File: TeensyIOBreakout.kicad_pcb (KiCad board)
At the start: 2 copper layers, 41 x 32.5 mm, 9 parts, among them J1 Conn_01x14_Male, J2 Conn_01x14_Male, J3 Conn_01x14_Male, J4 Conn_01x14_Male, J5 Conn_01x03_Male, J6 Conn_01x05_Male, J7 Conn_01x02_Male, U1 Teensy3.2

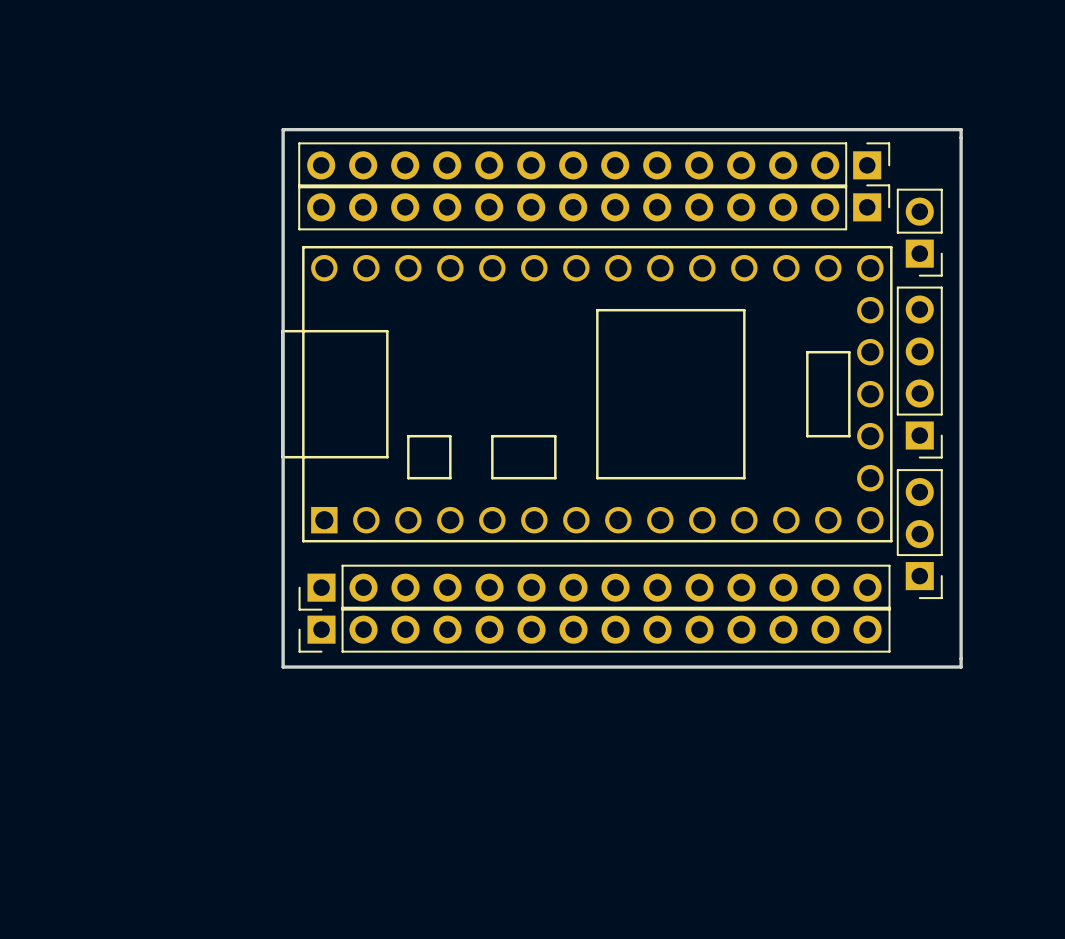
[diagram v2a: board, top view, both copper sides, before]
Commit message: Made board bigger, added moutning holes, front labels
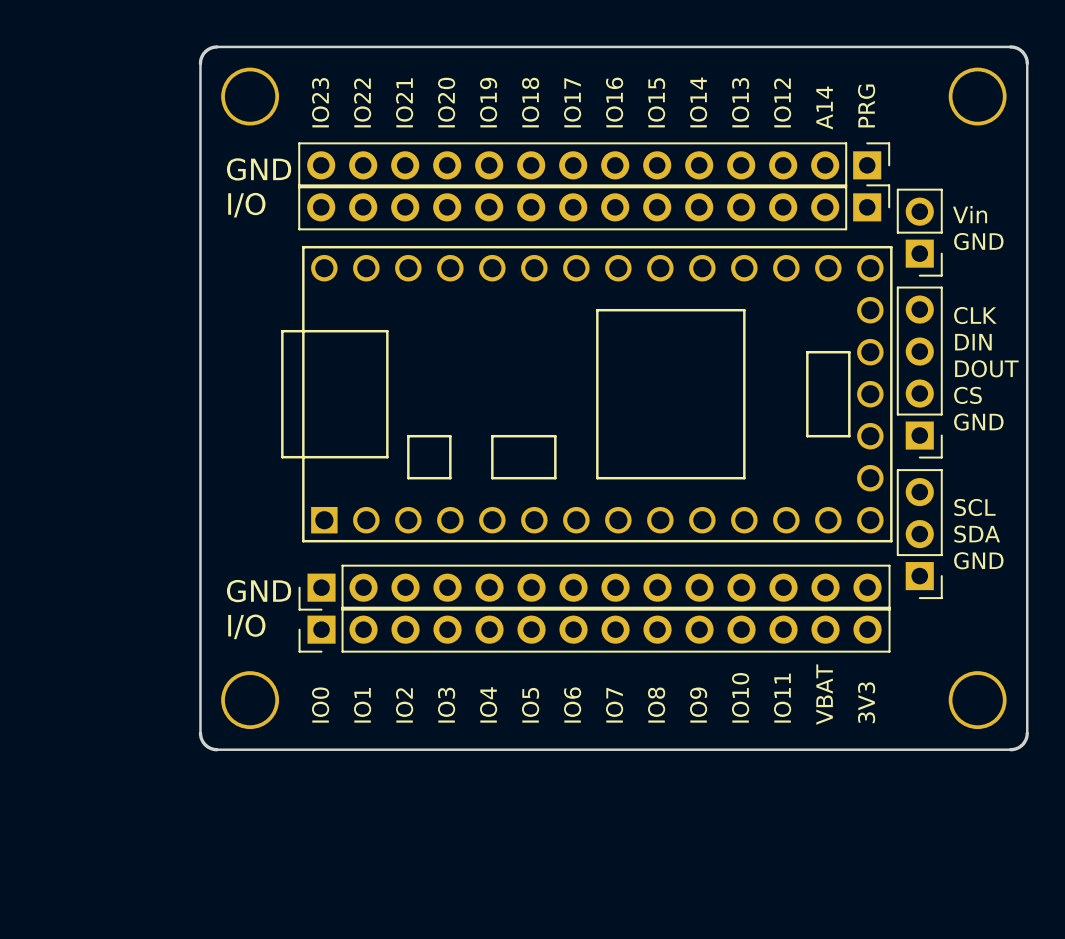
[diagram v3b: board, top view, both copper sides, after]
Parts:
- added REF**: mount, mount:mount, F.Cu at (153.0, 57.0)
- added REF**: mount, mount:mount, F.Cu at (153.0, 20.5)
- added REF**: mount, mount:mount, F.Cu at (109.0, 20.5)
- added REF**: mount, mount:mount, F.Cu at (109.0, 57.0)
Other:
- board size 41 x 32.5 mm -> 50 x 42.5 mm
- board text added: "3V3"
- board text added: "A14"
- board text added: "CLK DIN DOUT CS GND"
- board text added: "GND I/O"
- board text added: "IO0"
- board text added: "IO1"
- board text added: "IO10"
- board text added: "IO11"
- board text added: "IO12"
- board text added: "IO13"
- board text added: "IO14"
- board text added: "IO15"
- board text added: "IO16"
- board text added: "IO17"
- board text added: "IO18"
- board text added: "IO19"
- board text added: "IO2"
- board text added: "IO20"
- board text added: "IO21"
- board text added: "IO22"
- board text added: "IO23"
- board text added: "IO3"
- board text added: "IO4"
- board text added: "IO5"
- board text added: "IO6"
- board text added: "IO7"
- board text added: "IO8"
- board text added: "IO9"
- board text added: "PRG"
- board text added: "SCL SDA GND"
- board text added: "VBAT"
- board text added: "Vin GND"
- board text removed: "Cl.Da.G"
- board text removed: "Cl.Di.Do.Cs.G"
- board text removed: "IO0 \/ IO11 VBAT 3V3"
- board text removed: "IO23 \/ IO12 A14 PROG"
- board text removed: "Vin.G"
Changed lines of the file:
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@@
   (general
     (thickness 1.6)
-    (drawings 13)
+    (drawings 41)
     (tracks 0)
     (zones 0)
-    (modules 9)
+    (modules 13)
     (nets 34)
   )
@@
     (mod_text_size 1 1)
     (mod_text_width 0.15)
-    (pad_size 1.524 1.524)
-    (pad_drill 0.762)
+    (pad_size 3.5 3.5)
+    (pad_drill 3.048)
     (pad_to_mask_clearance 0.2)
     (aux_axis_origin 0 0)
@@
     (add_net VBAT)
     (add_net Vin)
+  )
+  (module mount:mount (layer F.Cu)
+    (at 153 57)
+    (descr "3mm mount hole for 5.25mm standoff")
+    (tags DEV)
+    (fp_text reference REF** (at 0 -3.048) (layer F.SilkS) hide
+      (effects (font (size 1 1) (thickness 0.15)))
+    )
+    (fp_text value mount (at 0 3) (layer F.Fab) hide
+      (effects (font (size 1 1) (thickness 0.15)))
+    )
+    (fp_circle (center 0 0) (end 2.6 0) (layer F.CrtYd) (width 0.05))
+    (pad "" thru_hole circle (at 0 0) (size 3.5 3.5) (drill 3.048) (layers *.Cu *.Mask))
+  )
+  (module mount:mount (layer F.Cu)
+    (at 153 20.5)
+    (descr "3mm mount hole for 5.25mm standoff")
+    (tags DEV)
+    (fp_text reference REF** (at 0 -3.048) (layer F.SilkS) hide
+      (effects (font (size 1 1) (thickness 0.15)))
+    )
+    (fp_text value mount (at 0 3) (layer F.Fab) hide
+      (effects (font (size 1 1) (thickness 0.15)))
+    )
+    (fp_circle (center 0 0) (end 2.6 0) (layer F.CrtYd) (width 0.05))
+    (pad "" thru_hole circle (at 0 0) (size 3.5 3.5) (drill 3.048) (layers *.Cu *.Mask))
+  )
+  (module mount:mount (layer F.Cu)
+    (at 109 20.5)
+    (descr "3mm mount hole for 5.25mm standoff")
+    (tags DEV)
+    (fp_text reference REF** (at 0 -3.048) (layer F.SilkS) hide
+      (effects (font (size 1 1) (thickness 0.15)))
+    )
+    (fp_text value mount (at 0 3) (layer F.Fab) hide
+      (effects (font (size 1 1) (thickness 0.15)))
+    )
+    (fp_circle (center 0 0) (end 2.6 0) (layer F.CrtYd) (width 0.05))
+    (pad "" thru_hole circle (at 0 0) (size 3.5 3.5) (drill 3.048) (layers *.Cu *.Mask))
   )
   (module Pin_Headers:Pin_Header_Straight_1x14_Pitch2.54mm (layer F.Cu)
@@
       (xy 0.280132 4.064859)) (layer B.SilkS) (width 0.01))
   )
-  (gr_text Vin.G (at 144 35 90) (layer B.SilkS)
-    (effects (font (size 1.1 1) (thickness 0.2)) (justify mirror))
-  )
-  (gr_text Cl.Di.Do.Cs.G (at 142 38.5 90) (layer B.SilkS)
-    (effects (font (size 1.1 1) (thickness 0.2)) (justify mirror))
-  )
-  (gr_text Cl.Da.G (at 144 42 90) (layer B.SilkS)
-    (effects (font (size 1.1 1) (thickness 0.2)) (justify mirror))
-  )
-  (gr_text "IO0\n\\/\nIO11\nVBAT\n3V3" (at 130 42.5 90) (layer B.SilkS)
-    (effects (font (size 1.1 1.1) (thickness 0.2)) (justify mirror))
-  )
-  (gr_text "IO23\n\\/\nIO12\nA14\nPROG" (at 130 34.5 90) (layer B.SilkS)
-    (effects (font (size 1.1 1.1) (thickness 0.2)) (justify mirror))
-  )
-  (dimension 41 (width 0.3) (layer Dwgs.User)
-    (gr_text "41.000 mm" (at 131.5 18.9) (layer Dwgs.User)
-      (effects (font (size 1.5 1.5) (thickness 0.3)))
-    )
-    (feature1 (pts (xy 152 22.5) (xy 152 20.413579)))
-    (feature2 (pts (xy 111 22.5) (xy 111 20.413579)))
-    (crossbar (pts (xy 111 21) (xy 152 21)))
-    (arrow1a (pts (xy 152 21) (xy 150.873496 21.586421)))
-    (arrow1b (pts (xy 152 21) (xy 150.873496 20.413579)))
-    (arrow2a (pts (xy 111 21) (xy 112.126504 21.586421)))
-    (arrow2b (pts (xy 111 21) (xy 112.126504 20.413579)))
-  )
-  (dimension 32.5 (width 0.3) (layer Dwgs.User)
-    (gr_text "32.500 mm" (at 156.1 38.75 270) (layer Dwgs.User)
-      (effects (font (size 1.5 1.5) (thickness 0.3)))
-    )
-    (feature1 (pts (xy 152 55) (xy 154.586421 55)))
-    (feature2 (pts (xy 152 22.5) (xy 154.586421 22.5)))
-    (crossbar (pts (xy 154 22.5) (xy 154 55)))
-    (arrow1a (pts (xy 154 55) (xy 153.413579 53.873496)))
-    (arrow1b (pts (xy 154 55) (xy 154.586421 53.873496)))
-    (arrow2a (pts (xy 154 22.5) (xy 153.413579 23.626504)))
-    (arrow2b (pts (xy 154 22.5) (xy 154.586421 23.626504)))
-  )
-  (gr_line (start 152 22.5) (end 152 23) (layer Edge.Cuts) (width 0.2))
-  (gr_line (start 111 22.5) (end 152 22.5) (layer Edge.Cuts) (width 0.2))
-  (gr_line (start 111 55) (end 111 22.5) (layer Edge.Cuts) (width 0.2))
-  (gr_line (start 152 55) (end 111 55) (layer Edge.Cuts) (width 0.2))
-  (gr_line (start 152 54.5) (end 152 55) (layer Edge.Cuts) (width 0.2))
-  (gr_line (start 152 23) (end 152 54.5) (layer Edge.Cuts) (width 0.2))
+  (module mount:mount (layer F.Cu)
+    (at 109 57)
+    (descr "3mm mount hole for 5.25mm standoff")
+    (tags DEV)
+    (fp_text reference REF** (at 0 -3.048) (layer F.SilkS) hide
+      (effects (font (size 1 1) (thickness 0.15)))
+    )
+    (fp_text value mount (at 0 3) (layer F.Fab) hide
+      (effects (font (size 1 1) (thickness 0.15)))
+    )
+    (fp_circle (center 0 0) (end 2.6 0) (layer F.CrtYd) (width 0.05))
+    (pad "" thru_hole circle (at 0 0) (size 3.5 3.5) (drill 3.048) (layers *.Cu *.Mask))
+  )
+  (gr_text "IO8\n" (at 133.62 58.5 90) (layer F.SilkS)
+    (effects (font (size 1 1) (thickness 0.175)) (justify left))
+  )
+  (gr_text "IO9\n" (at 136.16 58.5 90) (layer F.SilkS)
+    (effects (font (size 1 1) (thickness 0.175)) (justify left))
+  )
+  (gr_text "IO11\n" (at 141.24 58.5 90) (layer F.SilkS)
+    (effects (font (size 1 1) (thickness 0.175)) (justify left))
+  )
+  (gr_text 3V3 (at 146.32 58.5 90) (layer F.SilkS)
+    (effects (font (size 1 1) (thickness 0.175)) (justify left))
+  )
+  (gr_text IO7 (at 131.08 58.5 90) (layer F.SilkS)
+    (effects (font (size 1 1) (thickness 0.175)) (justify left))
+  )
+  (gr_text "IO10\n" (at 138.7 58.5 90) (layer F.SilkS)
+    (effects (font (size 1 1) (thickness 0.175)) (justify left))
+  )
+  (gr_text "IO4\n" (at 123.46 58.5 90) (layer F.SilkS)
+    (effects (font (size 1 1) (thickness 0.175)) (justify left))
+  )
+  (gr_text VBAT (at 143.78 58.5 90) (layer F.SilkS)
+    (effects (font (size 1 1) (thickness 0.175)) (justify left))
+  )
+  (gr_text IO6 (at 128.54 58.5 90) (layer F.SilkS)
+    (effects (font (size 1 1) (thickness 0.175)) (justify left))
+  )
+  (gr_text IO5 (at 126 58.5 90) (layer F.SilkS)
+    (effects (font (size 1 1) (thickness 0.175)) (justify left))
+  )
+  (gr_text IO2 (at 118.38 58.5 90) (layer F.SilkS)
+    (effects (font (size 1 1) (thickness 0.175)) (justify left))
+  )
+  (gr_text "IO3\n" (at 120.92 58.5 90) (layer F.SilkS)
+    (effects (font (size 1 1) (thickness 0.175)) (justify left))
+  )
+  (gr_text "IO1\n" (at 115.84 58.5 90) (layer F.SilkS)
+    (effects (font (size 1 1) (thickness 0.175)) (justify left))
+  )
+  (gr_text "IO0\n" (at 113.3 58.5 90) (layer F.SilkS)
+    (effects (font (size 1 1) (thickness 0.175)) (justify left))
+  )
+  (gr_text PRG (at 146.32 22.5 90) (layer F.SilkS)
+    (effects (font (size 1 1) (thickness 0.175)) (justify left))
+  )
+  (gr_text A14 (at 143.78 22.5 90) (layer F.SilkS)
+    (effects (font (size 1 1) (thickness 0.175)) (justify left))
+  )
+  (gr_text "IO12\n" (at 141.24 22.5 90) (layer F.SilkS)
+    (effects (font (size 1 1) (thickness 0.175)) (justify left))
+  )
+  (gr_text "IO13\n" (at 138.7 22.5 90) (layer F.SilkS)
+    (effects (font (size 1 1) (thickness 0.175)) (justify left))
+  )
+  (gr_text "IO14\n" (at 136.16 22.5 90) (layer F.SilkS)
+    (effects (font (size 1 1) (thickness 0.175)) (justify left))
+  )
+  (gr_text "IO15\n" (at 133.62 22.5 90) (layer F.SilkS)
+    (effects (font (size 1 1) (thickness 0.175)) (justify left))
+  )
+  (gr_text "IO16\n" (at 131.08 22.5 90) (layer F.SilkS)
+    (effects (font (size 1 1) (thickness 0.175)) (justify left))
+  )
+  (gr_text IO17 (at 128.54 22.5 90) (layer F.SilkS)
+    (effects (font (size 1 1) (thickness 0.175)) (justify left))
+  )
+  (gr_text "IO18\n" (at 126 22.5 90) (layer F.SilkS)
+    (effects (font (size 1 1) (thickness 0.175)) (justify left))
+  )
+  (gr_text "IO19\n" (at 123.46 22.5 90) (layer F.SilkS)
+    (effects (font (size 1 1) (thickness 0.175)) (justify left))
+  )
+  (gr_text "IO20\n" (at 120.92 22.5 90) (layer F.SilkS)
+    (effects (font (size 1 1) (thickness 0.175)) (justify left))
+  )
+  (gr_text "IO21\n" (at 118.38 22.5 90) (layer F.SilkS)
+    (effects (font (size 1 1) (thickness 0.175)) (justify left))
+  )
+  (gr_text "IO22\n" (at 115.84 22.5 90) (layer F.SilkS)
+    (effects (font (size 1 1) (thickness 0.175)) (justify left))
+  )
+  (gr_text "IO23\n" (at 113.3 22.5 90) (layer F.SilkS)
+    (effects (font (size 1 1) (thickness 0.175)) (justify left))
+  )
+  (gr_text "GND\nI/O" (at 107.5 51.5) (layer F.SilkS)
+    (effects (font (size 1.3 1.3) (thickness 0.2)) (justify left))
+  )
+  (gr_text "GND\nI/O" (at 107.5 26) (layer F.SilkS)
+    (effects (font (size 1.3 1.3) (thickness 0.2)) (justify left))
+  )
+  (gr_text "CLK\nDIN\nDOUT\nCS\nGND" (at 151.5 37) (layer F.SilkS)
+    (effects (font (size 1 1) (thickness 0.175)) (justify left))
+  )
+  (gr_text "SCL\nSDA\nGND" (at 151.5 47) (layer F.SilkS)
+    (effects (font (size 1 1) (thickness 0.175)) (justify left))
+  )
+  (gr_line (start 106 18.5) (end 106 59) (layer Edge.Cuts) (width 0.15))
+  (gr_line (start 155 17.5) (end 107 17.5) (layer Edge.Cuts) (width 0.15))
+  (gr_line (start 156 59) (end 156 18.5) (layer Edge.Cuts) (width 0.15))
+  (gr_line (start 107 60) (end 155 60) (layer Edge.Cuts) (width 0.15))
+  (gr_arc (start 107 59) (end 106 59) (angle -90) (layer Edge.Cuts) (width 0.2))
+  (gr_arc (start 107 18.5) (end 107 17.5) (angle -90) (layer Edge.Cuts) (width 0.2))
+  (gr_arc (start 155 18.5) (end 156 18.5) (angle -90) (layer Edge.Cuts) (width 0.2))
+  (gr_arc (start 155 59) (end 155 60) (angle -90) (layer Edge.Cuts) (width 0.2))
+  (gr_text "Vin\nGND" (at 151.5 28.5) (layer F.SilkS)
+    (effects (font (size 1 1) (thickness 0.2)) (justify left))
+  )
 )

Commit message: Added USB cutout, fixed labels.
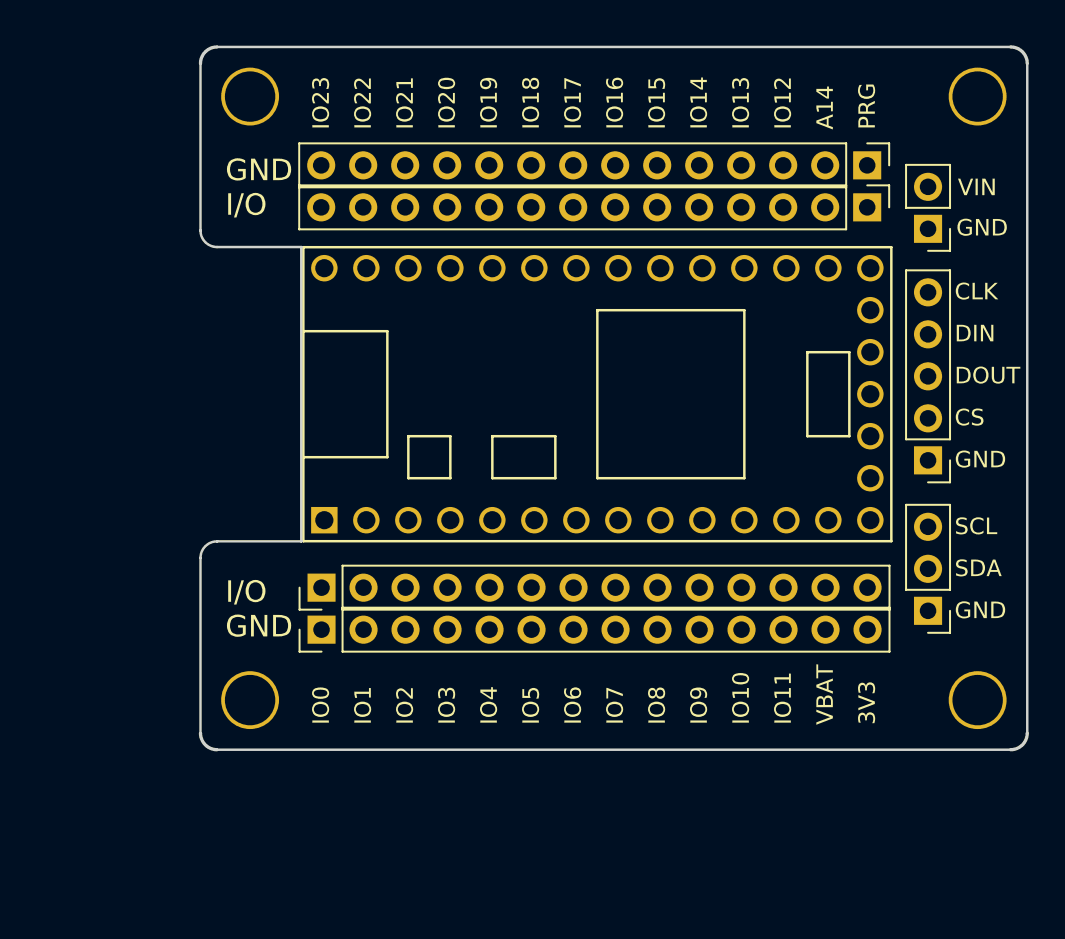
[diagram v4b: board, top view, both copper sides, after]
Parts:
- J6: footprint Pin_Headers:Pin_Header_Straight_1x04_Pitch2.54mm -> Pin_Headers:Pin_Header_Straight_1x05_Pitch2.54mm
- moved J5 2.16 mm to (150.0, 51.6)
- moved J6 1.58 mm to (150.0, 42.5)
- moved J7 1.58 mm to (150.0, 28.5)
- moved G*** 0.67 mm to (119.9, 38.2), turned to 180 degrees
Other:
- outline, holes or cut-outs redrawn
- board text added: "CLK"
- board text added: "CS"
- board text added: "DIN"
- board text added: "DOUT"
- board text added: "GND"
- board text added: "I/O GND"
- board text added: "Maniacal Labs Teensy LC/3.1/2 I/O Breakout Board"
- board text added: "SCL"
- board text added: "SDA"
- board text added: "VIN"
- board text removed: "CLK DIN DOUT CS GND"
- board text removed: "SCL SDA GND"
- board text removed: "Vin GND"

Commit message: routing :)
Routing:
- net Vin: track 0.00 -> 49.1 mm
- net IO_18: track 0.00 -> 38.5 mm, vias 0 -> 1
- net IO_19: track 0.00 -> 37.9 mm
- net IO_12: track 0.00 -> 33.8 mm
- net IO_11: track 0.00 -> 18.9 mm, vias 0 -> 2
- net IO_10: track 0.00 -> 18.0 mm
- net IO_13: track 0.00 -> 13.4 mm
- net 3V3: track 0.00 -> 10.5 mm
- net PROG: track 0.00 -> 9.99 mm
- net IO_23: track 0.00 -> 9.57 mm
- net IO_14: track 0.00 -> 9.37 mm
- net IO_17: track 0.00 -> 9.33 mm
- net IO_15: track 0.00 -> 9.33 mm
- net IO_22: track 0.00 -> 9.33 mm
- net IO_21: track 0.00 -> 9.33 mm
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- added copper zone on B.Cu, net GND
- added copper zone on F.Cu, net GND
